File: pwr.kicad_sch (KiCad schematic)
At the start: 25 parts, among them U2 AMS1117-3.3, U4 TPS54336ADDA

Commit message: Clean up
Minor fixes to mistakes in the schematic
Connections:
- net GND: now also R5.2
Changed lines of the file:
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@@
+	(symbol
+		(lib_id "power:GND")
+		(at 153.67 31.75 0)
+		(unit 1)
+		(body_style 1)
+		(exclude_from_sim no)
+		(in_bom yes)
+		(on_board yes)
+		(in_pos_files yes)
+		(dnp no)
+		(fields_autoplaced yes)
+		(property "Reference" "#PWR019"
+			(at 153.67 38.1 0)
+			(hide yes)
+			(show_name no)
+			(do_not_autoplace no)
+			(effects
+				(font
+					(size 1.27 1.27)
+				)
+			)
+		)
+		(property "Value" "GND"
+			(at 153.67 36.83 0)
+			(show_name no)
+			(do_not_autoplace no)
+			(effects
+				(font
+					(size 1.27 1.27)
+				)
+			)
+		)
+		(property "Footprint" ""
+			(at 153.67 31.75 0)
+			(hide yes)
+			(show_name no)
+			(do_not_autoplace no)
+			(effects
+				(font
+					(size 1.27 1.27)
+				)
+			)
+		)
+		(property "Datasheet" ""
+			(at 153.67 31.75 0)
+			(hide yes)
+			(show_name no)
+			(do_not_autoplace no)
+			(effects
+				(font
+					(size 1.27 1.27)
+				)
+			)
+		)
+		(property "Description" "Power symbol creates a global label with name \"GND\" , ground"
+			(at 153.67 31.75 0)
+			(hide yes)
+			(show_name no)
+			(do_not_autoplace no)
+			(effects
+				(font
+					(size 1.27 1.27)
+				)
+			)
+		)
+		(pin "1"
+		)
+		(instances
+			(project "X19-Float-Board"
+				(path "/00000000-0000-0000-0000-000060e6118b/dfdc99bd-6797-4c58-8fa3-5fd2e2701b4c"
+					(reference "#PWR019")
+					(unit 1)
+				)
+			)
+		)
+	)
 	(symbol
 		(lib_id "power:GND")

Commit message: Gave footprints to everything
Footprints
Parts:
- C1, C2, C3, C4, C5, C6, C7, C8, L1: footprint (none) -> Capacitor_SMD:C_0603_1608Metric
- F1: footprint (none) -> Fuse:Fuse_1812_4532Metric
- R1, R2, R3, R4, R5: footprint (none) -> Resistor_SMD:R_0603_1608Metric
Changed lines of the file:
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@@
 			)
 		)
-		(property "Footprint" ""
+		(property "Footprint" "Fuse:Fuse_1812_4532Metric"
 			(at 51.308 38.1 90)
 			(hide yes)
@@
 			)
 		)
-		(property "Footprint" ""
+		(property "Footprint" "Capacitor_SMD:C_0603_1608Metric"
 			(at 132.08 21.59 0)
 			(hide yes)
@@
 			)
 		)
-		(property "Footprint" ""
+		(property "Footprint" "Capacitor_SMD:C_0603_1608Metric"
 			(at 95.25 39.37 0)
 			(hide yes)
@@
 			)
 		)
-		(property "Footprint" ""
+		(property "Footprint" "Resistor_SMD:R_0603_1608Metric"
 			(at 153.67 24.13 0)
 			(hide yes)
@@
 			)
 		)
-		(property "Footprint" ""
+		(property "Footprint" "Capacitor_SMD:C_0603_1608Metric"
 			(at 144.78 24.13 0)
 			(hide yes)
@@
 			)
 		)
-		(property "Footprint" ""
+		(property "Footprint" "Capacitor_SMD:C_0603_1608Metric"
 			(at 86.36 21.59 0)
 			(hide yes)
@@
 			)
 		)
-		(property "Footprint" ""
+		(property "Footprint" "Capacitor_SMD:C_0603_1608Metric"
 			(at 125.73 21.59 0)
 			(hide yes)
@@
 			)
 		)
-		(property "Footprint" ""
+		(property "Footprint" "Capacitor_SMD:C_0603_1608Metric"
 			(at 95.25 29.21 0)
 			(hide yes)
@@
 			)
 		)
-		(property "Footprint" ""
+		(property "Footprint" "Capacitor_SMD:C_0603_1608Metric"
 			(at 135.89 24.13 0)
 			(hide yes)
@@
 			)
 		)
-		(property "Footprint" ""
+		(property "Footprint" "Resistor_SMD:R_0603_1608Metric"
 			(at 95.25 34.29 0)
 			(hide yes)
@@
 			)
 		)
-		(property "Footprint" ""
+		(property "Footprint" "Resistor_SMD:R_0603_1608Metric"
 			(at 69.85 25.4 0)
 			(hide yes)
@@
 			)
 		)
-		(property "Footprint" ""
+		(property "Footprint" "Capacitor_SMD:C_0603_1608Metric"
 			(at 87.63 34.29 0)
 			(hide yes)
@@
 			)
 		)
-		(property "Footprint" ""
+		(property "Footprint" "Capacitor_SMD:C_0603_1608Metric"
 			(at 77.47 21.59 0)
 			(hide yes)
@@
 			)
 		)
-		(property "Footprint" ""
+		(property "Footprint" "Resistor_SMD:R_0603_1608Metric"
 			(at 69.85 30.48 0)
 			(hide yes)
@@
 			)
 		)
-		(property "Footprint" ""
+		(property "Footprint" "Resistor_SMD:R_0603_1608Metric"
 			(at 153.67 29.21 0)
 			(hide yes)

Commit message: Modifications to power system to support what is required
modified
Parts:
- removed BT2, BT3, BT4, BT5, BT6, BT7, BT8, BT9: 1.5V, symbol Device:Battery
- removed C3: 10µF, Capacitor_SMD:C_0603_1608Metric, symbol Device:C_Small
- removed C4: 120pF, Capacitor_SMD:C_0603_1608Metric, symbol Device:C_Small
- removed C5: .012µF, Capacitor_SMD:C_0603_1608Metric, symbol Device:C_Small
- removed C6: 0.1µF, Capacitor_SMD:C_0603_1608Metric, symbol Device:C_Small
- removed C7, C8: 47µF, Capacitor_SMD:C_0603_1608Metric, symbol Device:C_Small
- removed L1: 15µH, Capacitor_SMD:C_0603_1608Metric, symbol Device:L
- removed R1: 220kΩ, Resistor_SMD:R_0603_1608Metric, symbol Device:R_Small_US
- removed R2: 43.2kΩ, Resistor_SMD:R_0603_1608Metric, symbol Device:R_Small_US
- removed R3: 3.74kΩ, Resistor_SMD:R_0603_1608Metric, symbol Device:R_Small_US
- removed R4: 100051Ω, Resistor_SMD:R_0603_1608Metric, symbol Device:R_Small_US
- removed R5: 19.1kΩ, Resistor_SMD:R_0603_1608Metric, symbol Device:R_Small_US
- removed U2: AMS1117-3.3, Package_TO_SOT_SMD:SOT-223-3_TabPin2, symbol Regulator_Linear:AMS1117-3.3
- removed U4: TPS54336ADDA, Package_SO:TI_SO-PowerPAD-8_ThermalVias, symbol Regulator_Switching:TPS54336ADDA
- added D2: 1N5822, Diode_THT:D_DO-201AD_P15.24mm_Horizontal, symbol Diode:1N5822
- added J3: Screw_Terminal_01x02, TerminalBlock_Altech:Altech_AK100_1x02_P5.00mm, symbol Connector:Screw_Terminal_01x02
- added L1: 33µH, symbol Device:L_Small
- added U2: LM2596S-3.3, Package_TO_SOT_SMD:TO-263-5_TabPin3, symbol Regulator_Switching:LM2596S-3.3
- C1: value 100nF -> 220µF; footprint Capacitor_SMD:C_0603_1608Metric -> (none)
- C2: value 27nF -> 680µF; footprint Capacitor_SMD:C_0603_1608Metric -> (none)
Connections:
- net 12 V: now also C2.1, U2.1 (VIN); no longer C1.1
- net 3.3 V: now also C1.1, L1.2, U2.4 (FB)
- net GND: now also C2.2, D2.2 (A), J3.1 (Pin_1), U2.3 (GND), U2.5 (~{ON}/OFF); no longer C2.1
- net at F1.2: now also J3.2 (Pin_2)
- new net: D2.1 (K), L1.1, U2.2 (OUT)
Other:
- note added: "428284"

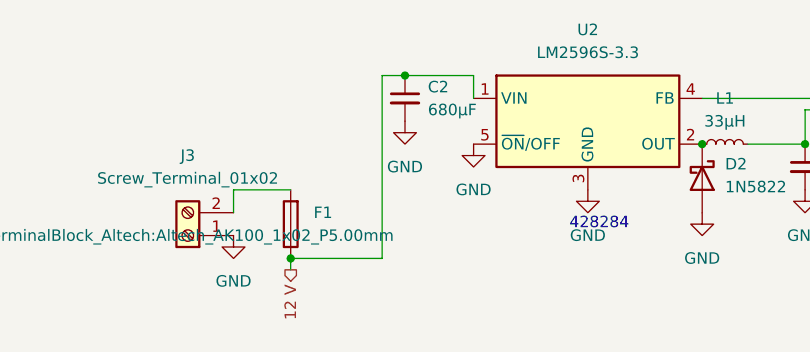
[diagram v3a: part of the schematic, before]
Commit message: Schematic updates
Schematic updates to match with pcb edits
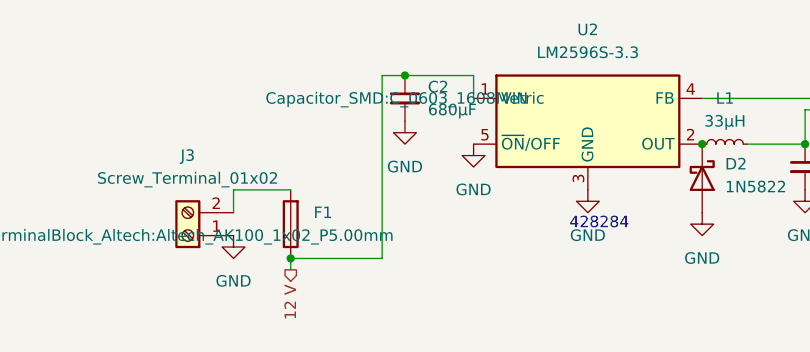
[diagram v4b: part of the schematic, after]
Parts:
- C1, C2: footprint (none) -> Capacitor_SMD:C_0603_1608Metric
- L1: footprint (none) -> Inductor_SMD:L_0603_1608Metric
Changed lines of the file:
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@@
 			)
 		)
-		(property "Footprint" ""
+		(property "Footprint" "Inductor_SMD:L_0603_1608Metric"
 			(at 97.79 29.21 0)
 			(hide yes)
@@
 			)
 		)
-		(property "Footprint" ""
+		(property "Footprint" "Capacitor_SMD:C_0603_1608Metric"
 			(at 106.68 31.75 0)
 			(hide yes)
@@
 			)
 		)
-		(property "Footprint" ""
+		(property "Footprint" "Capacitor_SMD:C_0603_1608Metric"
 			(at 62.23 24.13 0)
-			(hide yes)
-			(show_name no)
-			(do_not_autoplace no)
+			(show_name no)
+			(do_not_autoplace no)

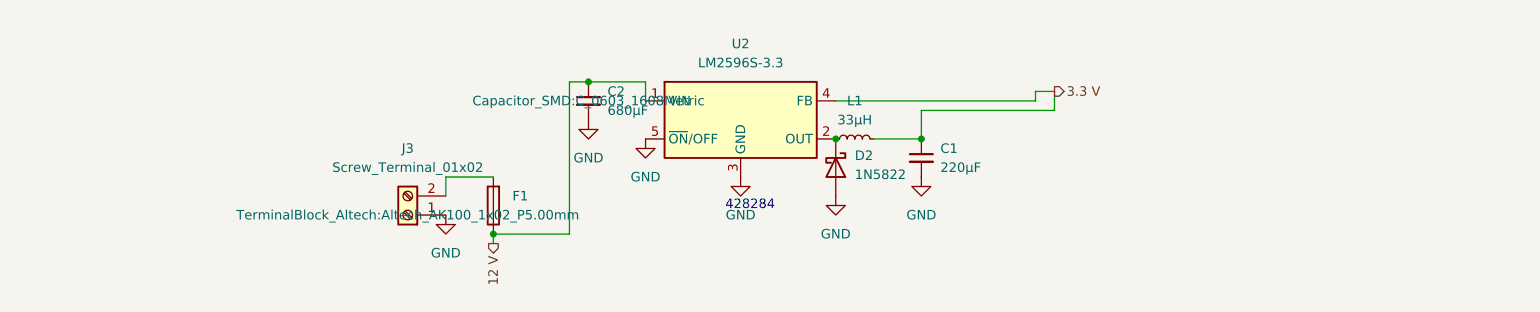
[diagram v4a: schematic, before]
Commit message: USB-C + Complete wiring
Compltetly wired the pcb (I don't understand the DRC errors) and added a usb C to flash the stm, modified the switch to be the BOOT0 for the stm so it controls whether the stm is in flash mode
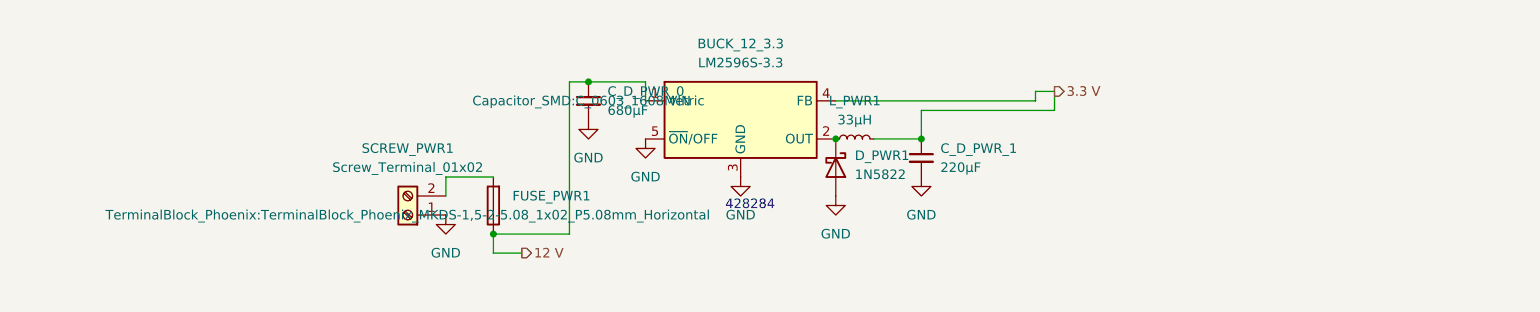
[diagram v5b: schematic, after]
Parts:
- SCREW_PWR1: renamed from J3; footprint TerminalBlock_Altech:Altech_AK100_1x02_P5.00mm -> TerminalBlock_Phoenix:TerminalBlock_Phoenix_MKDS-1,5-2-5.08_1x02_P5.08mm_Horizontal
- renumbered U2 to BUCK_12_3.3, C2 to C_D_PWR_0, C1 to C_D_PWR_1, D2 to D_PWR1, F1 to FUSE_PWR1, L1 to L_PWR1
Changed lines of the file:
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@@
 	(wire
 		(pts
-			(xy 49.53 43.18) (xy 49.53 41.91)
+			(xy 69.85 21.59) (xy 69.85 24.13)
 		)
 		(stroke
@@
 	(wire
 		(pts
-			(xy 69.85 21.59) (xy 69.85 24.13)
+			(xy 59.69 41.91) (xy 49.53 41.91)
 		)
 		(stroke
@@
 	(wire
 		(pts
-			(xy 59.69 41.91) (xy 49.53 41.91)
+			(xy 100.33 29.21) (xy 106.68 29.21)
 		)
 		(stroke
@@
 	(wire
 		(pts
-			(xy 100.33 29.21) (xy 106.68 29.21)
+			(xy 124.46 22.86) (xy 124.46 25.4)
 		)
 		(stroke
@@
 	(wire
 		(pts
-			(xy 124.46 22.86) (xy 124.46 25.4)
+			(xy 106.68 25.4) (xy 106.68 29.21)
 		)
 		(stroke
@@
 	(wire
 		(pts
-			(xy 106.68 25.4) (xy 106.68 29.21)
+			(xy 49.53 44.45) (xy 49.53 41.91)
 		)
 		(stroke
@@
 	(wire
 		(pts
-			(xy 121.92 24.13) (xy 95.25 24.13)
+			(xy 53.34 44.45) (xy 49.53 44.45)
 		)
 		(stroke
@@
 		)
 	)
+	(wire
+		(pts
+			(xy 121.92 24.13) (xy 95.25 24.13)
+		)
+		(stroke
+			(width 0)
+			(type default)
+		)
+	)
 	(hierarchical_label "12 V"
 		(shape output)
-		(at 49.53 43.18 270)
+		(at 53.34 44.45 0)
 		(effects
 			(font
 				(size 1.27 1.27)
 			)
-			(justify right)
+			(justify left)
 		)
 	)
@@
 		(dnp no)
 		(fields_autoplaced yes)
-		(property "Reference" "F1"
+		(property "Reference" "FUSE_PWR1"
 			(at 52.07 36.8299 0)
 			(show_name no)
@@
 			(project "X19-Float-Board"
 				(path "/00000000-0000-0000-0000-000060e6118b/dfdc99bd-6797-4c58-8fa3-5fd2e2701b4c"
-					(reference "F1")
+					(reference "FUSE_PWR1")
 					(unit 1)
 				)
@@
 		(dnp no)
 		(fields_autoplaced yes)
-		(property "Reference" "U2"
+		(property "Reference" "BUCK_12_3.3"
 			(at 82.55 16.51 0)
 			(show_name no)
@@
 			(project "X19-Float-Board"
 				(path "/00000000-0000-0000-0000-000060e6118b/dfdc99bd-6797-4c58-8fa3-5fd2e2701b4c"
-					(reference "U2")
+					(reference "BUCK_12_3.3")
 					(unit 1)
 				)
@@
 		(dnp no)
 		(fields_autoplaced yes)
-		(property "Reference" "J3"
+		(property "Reference" "SCREW_PWR1"
 			(at 38.1 30.48 0)
 			(show_name no)
@@
 			)
 		)
-		(property "Footprint" "TerminalBlock_Altech:Altech_AK100_1x02_P5.00mm"
+		(property "Footprint" "TerminalBlock_Phoenix:TerminalBlock_Phoenix_MKDS-1,5-2-5.08_1x02_P5.08mm_Horizontal"
 			(at 38.1 39.37 0)
 			(show_name no)
@@
 			(project "X19-Float-Board"
 				(path "/00000000-0000-0000-0000-000060e6118b/dfdc99bd-6797-4c58-8fa3-5fd2e2701b4c"
-					(reference "J3")
+					(reference "SCREW_PWR1")
 					(unit 1)
 				)
@@
 		(dnp no)
 		(fields_autoplaced yes)
-		(property "Reference" "L1"
+		(property "Reference" "L_PWR1"
 			(at 97.79 24.13 90)
 			(show_name no)
@@
 			(project "X19-Float-Board"
 				(path "/00000000-0000-0000-0000-000060e6118b/dfdc99bd-6797-4c58-8fa3-5fd2e2701b4c"
-					(reference "L1")
+					(reference "L_PWR1")
 					(unit 1)
 				)
@@
 		(dnp no)
 		(fields_autoplaced yes)
-		(property "Reference" "C1"
+		(property "Reference" "C_D_PWR_1"
 			(at 109.22 30.4862 0)
 			(show_name no)
@@
 			(project "X19-Float-Board"
 				(path "/00000000-0000-0000-0000-000060e6118b/dfdc99bd-6797-4c58-8fa3-5fd2e2701b4c"
-					(reference "C1")
+					(reference "C_D_PWR_1")
 					(unit 1)
 				)
@@
 		(dnp no)
 		(fields_autoplaced yes)
-		(property "Reference" "C2"
+		(property "Reference" "C_D_PWR_0"
 			(at 64.77 22.8662 0)
 			(show_name no)
@@
 			(project "X19-Float-Board"
 				(path "/00000000-0000-0000-0000-000060e6118b/dfdc99bd-6797-4c58-8fa3-5fd2e2701b4c"
-					(reference "C2")
+					(reference "C_D_PWR_0")
 					(unit 1)
 				)
@@
 		(dnp no)
 		(fields_autoplaced yes)
-		(property "Reference" "D2"
+		(property "Reference" "D_PWR1"
 			(at 97.79 31.4324 90)
 			(show_name no)
@@
 			(project "X19-Float-Board"
 				(path "/00000000-0000-0000-0000-000060e6118b/dfdc99bd-6797-4c58-8fa3-5fd2e2701b4c"
-					(reference "D2")
-					(unit 1)
-				)
+					(reference "D_PWR1")
+					(unit 1)
+				)
